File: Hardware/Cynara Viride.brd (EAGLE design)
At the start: 160 x 100 mm, 170 parts, among them Q1 TXC-7B, Q2 TXC-7WNEO, SW1 430181038816, SW2 , T1 PDTC143, T2 PDTC143, T3 PDTC143, T4 PDTC143, T5 PDTC143, U1 TM4C129EN, U2 MCP1826S 3V3, U3 LM4132 3V3, U4 XC6SLX9-3TQG, U5 M25P16-SO8, U6 MCP1826S 1V2, X1 EDGE 50p, X11 SOCK2X17, X12 SOCK2X17, X13 SOCK2X17, X2 EDGE 50p, X23 debug xilinx, X24 debug 10p, X3 EDGE 50p, X4 EDGE 50p, X5 MicroMatch 24, X6 , X7 SOCK2X17, X8 RJ45-LAN-10/100

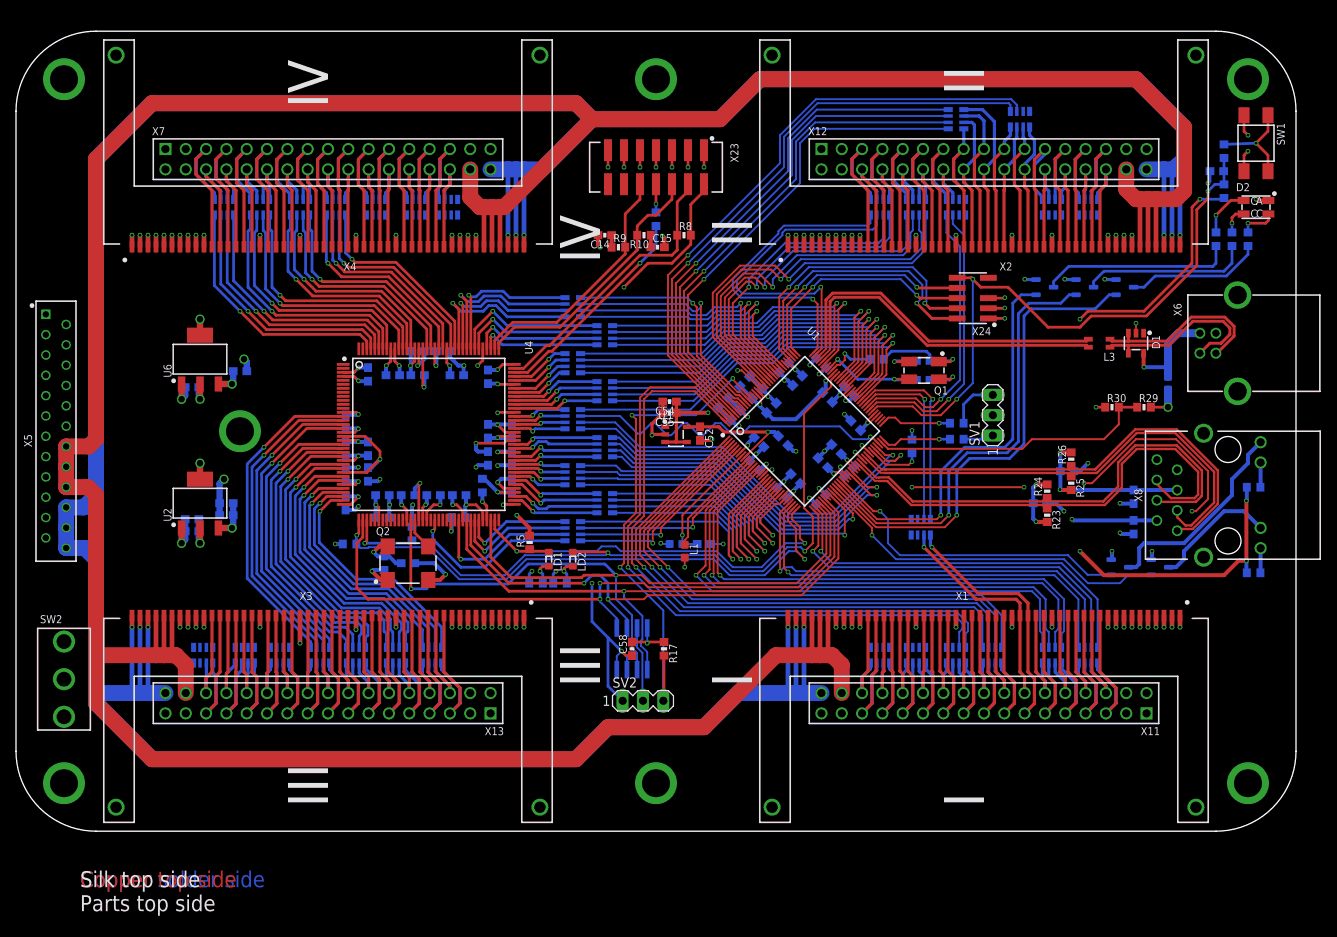
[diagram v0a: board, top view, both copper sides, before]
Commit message: Proper mounting holes. Small change in layout of +1.2V plane. Enhanced USB connector symbol. Added shield conenctions.
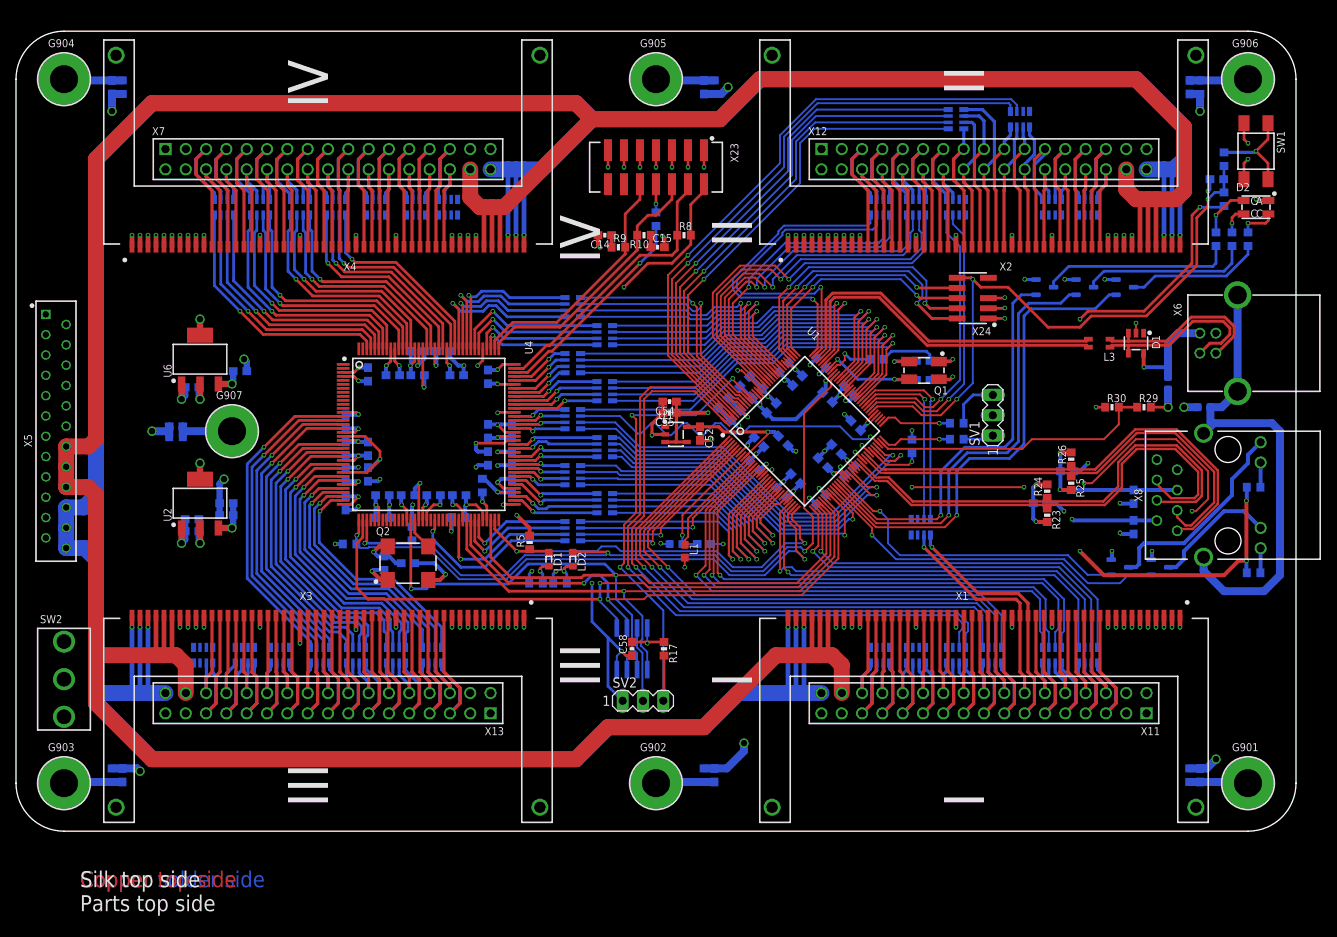
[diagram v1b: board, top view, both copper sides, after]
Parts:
- added C901, C902, C903, C904, C905, C906, C907: 100nF, Cynara-Passives:C0603
- added G901, G902, G903, G904, G905, G906, G907: (no value), Cynara-Misc:HOLE-3,5/6,6
- added L5: 26Z@100MHz, Cynara-Passives:L1608
- added R901, R902, R903, R904, R905, R906, R907: 1M, Cynara-Passives:R0603
- moved C51 1.00 mm to (150.1, 81.5)
- moved R13 1.00 mm to (151.0, 79.0)
- moved R14 1.00 mm to (151.0, 84.0)
- moved SW1 1.00 mm to (155.0, 85.0)
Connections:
- removed net P$1: X8.Z1, X8.Z2
- new net G901: C901.1, G901.1, R901.2
- new net G902: C902.1, G902.1, R902.2
- new net G903: C903.1, G903.1, R903.2
- new net G904: C904.1, G904.1, R904.2
- new net G905: C905.1, G905.1, R905.2
- new net G906: C906.1, G906.1, R906.2
- new net G907: C907.1, G907.1, R907.2
- new net SHIELD: L5.2, X6.Z1, X6.Z2, X8.Z1, X8.Z2
- net GND: now also C901.2, C902.2, C903.2, C904.2, C905.2, C906.2, C907.2, L5.1, R901.1, R902.1, R903.1, R904.1, R905.1, R906.1, R907.1
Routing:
- net SHIELD: track 0.00 -> 61.5 mm
- net GND: track 317.9 -> 347.6 mm, vias 129 -> 137
- net +1.2V: track 37.3 -> 55.5 mm
- net G907: track 0.00 -> 7.45 mm
- net G906: track 0.00 -> 7.36 mm
- net G901: track 0.00 -> 7.36 mm
- net G904: track 0.00 -> 7.36 mm
- net G903: track 0.00 -> 7.36 mm
- net G905: track 0.00 -> 7.36 mm
- net G902: track 0.00 -> 7.36 mm
- net !RST: track 79.2 -> 78.2 mm
- net +3.3V: track 279.2 -> 278.2 mm
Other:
- outline, holes or cut-outs redrawn

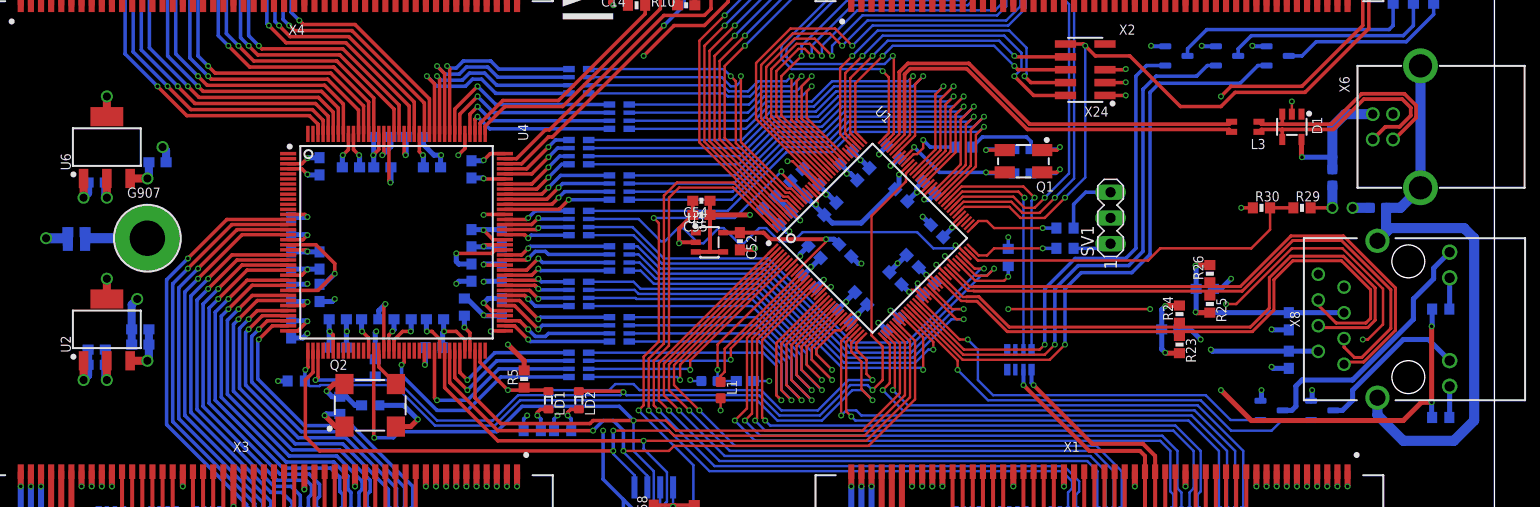
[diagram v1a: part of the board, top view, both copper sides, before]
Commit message: Changed microcontroller symbol to one a functional and power part. Renamed Petal signals. Shield for Ethernet and USB is a polygon now.
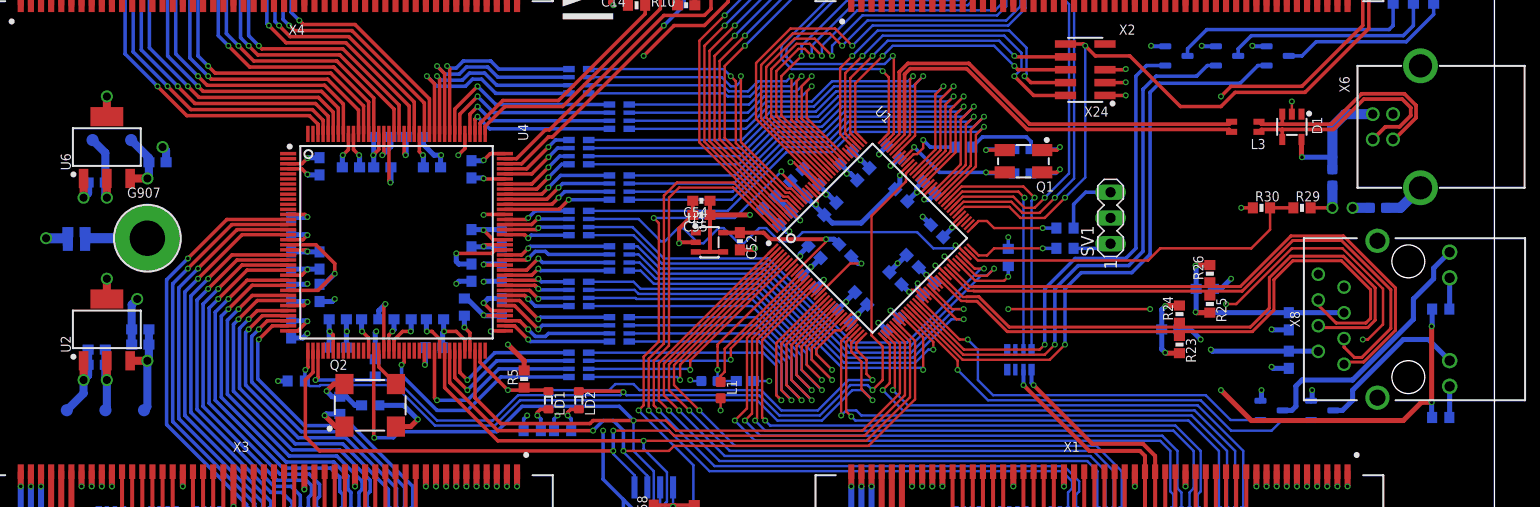
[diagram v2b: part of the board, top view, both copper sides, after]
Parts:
- added TP1, TP2, TP3, TP4, TP5: (no value), Cynara-Misc:TP-SMD
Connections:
- net FPGA_III_A renamed FPGA_III_1
- net FPGA_III_B renamed FPGA_III_2
- net FPGA_III_C renamed FPGA_III_3
- net FPGA_III_D renamed FPGA_III_4
- net FPGA_III_E renamed FPGA_III_5
- net FPGA_III_F renamed FPGA_III_6
- net FPGA_III_G renamed FPGA_III_7
- net FPGA_III_H renamed FPGA_III_8
- net FPGA_III_I renamed FPGA_III_9
- net FPGA_III_J renamed FPGA_III_10
- net FPGA_III_K renamed FPGA_III_11
- net FPGA_III_L renamed FPGA_III_12
- net FPGA_III_M renamed FPGA_III_13
- net FPGA_III_N renamed FPGA_III_14
- net FPGA_III_O renamed FPGA_III_15
- net FPGA_III_P renamed FPGA_III_16
- net FPGA_IV_A renamed FPGA_IV_1
- net FPGA_IV_B renamed FPGA_IV_2
- net FPGA_IV_C renamed FPGA_IV_3
- net FPGA_IV_D renamed FPGA_IV_4
- net FPGA_IV_E renamed FPGA_IV_5
- net FPGA_IV_F renamed FPGA_IV_6
- net FPGA_IV_G renamed FPGA_IV_7
- net FPGA_IV_H renamed FPGA_IV_8
- net FPGA_IV_I renamed FPGA_IV_9
- net FPGA_IV_J renamed FPGA_IV_10
- net FPGA_IV_K renamed FPGA_IV_11
- net FPGA_IV_L renamed FPGA_IV_12
- net FPGA_IV_M renamed FPGA_IV_13
- net FPGA_IV_N renamed FPGA_IV_14
- net FPGA_IV_O renamed FPGA_IV_15
- net FPGA_IV_P renamed FPGA_IV_16
- net MCU_II_A renamed MCU_II_1
- net MCU_II_B renamed MCU_II_2
- net MCU_II_C renamed MCU_II_3
- net MCU_II_D renamed MCU_II_4
- net MCU_II_E renamed MCU_II_5
- net MCU_II_F renamed MCU_II_6
- net MCU_II_G renamed MCU_II_7
- net MCU_II_H renamed MCU_II_8
- net MCU_II_I renamed MCU_II_9
- net MCU_II_J renamed MCU_II_10
- net MCU_II_K renamed MCU_II_11
- net MCU_II_L renamed MCU_II_12
- net MCU_II_M renamed MCU_II_13
- net MCU_II_N renamed MCU_II_14
- net MCU_II_O renamed MCU_II_15
- net MCU_II_P renamed MCU_II_16
- net MCU_I_A renamed MCU_I_1
- net MCU_I_B renamed MCU_I_2
- net MCU_I_C renamed MCU_I_3
- net MCU_I_D renamed MCU_I_4
- net MCU_I_E renamed MCU_I_5
- net MCU_I_F renamed MCU_I_6
- net MCU_I_G renamed MCU_I_7
- net MCU_I_H renamed MCU_I_8
- net MCU_I_I renamed MCU_I_9
- net MCU_I_J renamed MCU_I_10
- net MCU_I_K renamed MCU_I_11
- net MCU_I_L renamed MCU_I_12
- net MCU_I_M renamed MCU_I_13
- net MCU_I_N renamed MCU_I_14
- net MCU_I_O renamed MCU_I_15
- net MCU_I_P renamed MCU_I_16
- net N$10 renamed OSC1
- net N$7 renamed OSC0
- net N$79 renamed VDDA
- net N$84 renamed GNDA
- net PETAL_III_A renamed PETAL_III_1
- net PETAL_III_B renamed PETAL_III_2
- net PETAL_III_C renamed PETAL_III_3
- net PETAL_III_D renamed PETAL_III_4
- net PETAL_III_E renamed PETAL_III_5
- net PETAL_III_F renamed PETAL_III_6
- net PETAL_III_G renamed PETAL_III_7
- net PETAL_III_H renamed PETAL_III_8
- net PETAL_III_I renamed PETAL_III_9
- net PETAL_III_J renamed PETAL_III_10
- net PETAL_III_K renamed PETAL_III_11
- net PETAL_III_L renamed PETAL_III_12
- net PETAL_III_M renamed PETAL_III_13
- net PETAL_III_N renamed PETAL_III_14
- net PETAL_III_O renamed PETAL_III_15
- net PETAL_III_P renamed PETAL_III_16
- net PETAL_III_Q renamed PETAL_III_17
- net PETAL_III_R renamed PETAL_III_18
- net PETAL_III_S renamed PETAL_III_19
- net PETAL_III_T renamed PETAL_III_20
- net PETAL_III_U renamed PETAL_III_21
- net PETAL_III_V renamed PETAL_III_22
- net PETAL_III_W renamed PETAL_III_23
- net PETAL_III_X renamed PETAL_III_24
- net PETAL_III_Y renamed PETAL_III_25
- net PETAL_III_Z renamed PETAL_III_26
- net PETAL_II_A renamed PETAL_II_1
- net PETAL_II_B renamed PETAL_II_2
- net PETAL_II_C renamed PETAL_II_3
- net PETAL_II_D renamed PETAL_II_4
- net PETAL_II_E renamed PETAL_II_5
- net PETAL_II_F renamed PETAL_II_6
- net PETAL_II_G renamed PETAL_II_7
- net PETAL_II_H renamed PETAL_II_8
- net PETAL_II_I renamed PETAL_II_9
- net PETAL_II_J renamed PETAL_II_10
- net PETAL_II_K renamed PETAL_II_11
- net PETAL_II_L renamed PETAL_II_12
- net PETAL_II_M renamed PETAL_II_13
- net PETAL_II_N renamed PETAL_II_14
- net PETAL_II_O renamed PETAL_II_15
- net PETAL_II_P renamed PETAL_II_16
- net PETAL_II_Q renamed PETAL_II_17
- net PETAL_II_R renamed PETAL_II_18
- net PETAL_II_S renamed PETAL_II_19
- net PETAL_II_T renamed PETAL_II_20
- net PETAL_II_U renamed PETAL_II_21
- net PETAL_II_V renamed PETAL_II_22
- net PETAL_II_W renamed PETAL_II_23
- net PETAL_II_X renamed PETAL_II_24
- net PETAL_II_Y renamed PETAL_II_25
- net PETAL_II_Z renamed PETAL_II_26
- net PETAL_IV_A renamed PETAL_IV_1
- net PETAL_IV_B renamed PETAL_IV_2
- net PETAL_IV_C renamed PETAL_IV_3
- net PETAL_IV_D renamed PETAL_IV_4
- net PETAL_IV_E renamed PETAL_IV_5
- net PETAL_IV_F renamed PETAL_IV_6
- net PETAL_IV_G renamed PETAL_IV_7
- net PETAL_IV_H renamed PETAL_IV_8
- net PETAL_IV_I renamed PETAL_IV_9
- net PETAL_IV_J renamed PETAL_IV_10
- net PETAL_IV_K renamed PETAL_IV_11
- net PETAL_IV_L renamed PETAL_IV_12
- net PETAL_IV_M renamed PETAL_IV_13
- net PETAL_IV_N renamed PETAL_IV_14
- net PETAL_IV_O renamed PETAL_IV_15
- net PETAL_IV_P renamed PETAL_IV_16
- net PETAL_IV_Q renamed PETAL_IV_17
- net PETAL_IV_R renamed PETAL_IV_18
- net PETAL_IV_S renamed PETAL_IV_19
- net PETAL_IV_T renamed PETAL_IV_20
- net PETAL_IV_U renamed PETAL_IV_21
- net PETAL_IV_V renamed PETAL_IV_22
- net PETAL_IV_W renamed PETAL_IV_23
- net PETAL_IV_X renamed PETAL_IV_24
- net PETAL_IV_Y renamed PETAL_IV_25
- net PETAL_IV_Z renamed PETAL_IV_26
- net PETAL_I_A renamed PETAL_I_1
- net PETAL_I_B renamed PETAL_I_2
- net PETAL_I_C renamed PETAL_I_3
- net PETAL_I_D renamed PETAL_I_4
- net PETAL_I_E renamed PETAL_I_5
- net PETAL_I_F renamed PETAL_I_6
- net PETAL_I_G renamed PETAL_I_7
- net PETAL_I_H renamed PETAL_I_8
- net PETAL_I_I renamed PETAL_I_9
- net PETAL_I_J renamed PETAL_I_10
- net PETAL_I_K renamed PETAL_I_11
- net PETAL_I_L renamed PETAL_I_12
- net PETAL_I_M renamed PETAL_I_13
- net PETAL_I_N renamed PETAL_I_14
- net PETAL_I_O renamed PETAL_I_15
- net PETAL_I_P renamed PETAL_I_16
- net PETAL_I_Q renamed PETAL_I_17
- net PETAL_I_R renamed PETAL_I_18
- net PETAL_I_S renamed PETAL_I_19
- net PETAL_I_T renamed PETAL_I_20
- net PETAL_I_U renamed PETAL_I_21
- net PETAL_I_V renamed PETAL_I_22
- net PETAL_I_W renamed PETAL_I_23
- net PETAL_I_X renamed PETAL_I_24
- net PETAL_I_Y renamed PETAL_I_25
- net PETAL_I_Z renamed PETAL_I_26
- net VDCC renamed VDDC
- removed net FREE: U1.116
- removed net OLED_CS: U4.1
- removed net OLED_DC: U4.5
- removed net OLED_MOSI: U4.7
- removed net OLED_RST: U4.2
- removed net OLED_SCLK: U4.6
- removed net SH: X8.8
- net +1.2V: now also TP3.1
- net +3.3V: now also TP2.1
- net +5V: now also TP1.1
- net GND: now also TP4.1, TP5.1, X8.8
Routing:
- net SHIELD: track 61.5 -> 4.22 mm
- net GND: track 347.6 -> 359.8 mm, vias 137 -> 136
- net +3.3V: track 278.2 -> 284.5 mm
- net +5V: track 39.4 -> 43.1 mm
- net +1.2V: track 55.5 -> 58.4 mm
- net MCU_I_15: track 82.6 -> 81.7 mm
- net VDDC: track 17.9 -> 18.5 mm
- added copper zone on layer 15, net SHIELD
